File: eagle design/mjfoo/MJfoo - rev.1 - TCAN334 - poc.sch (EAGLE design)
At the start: 3 parts, among them J1 CAN, J2 Power Supply

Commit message: - updated MJfoo to rev. 1a
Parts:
- added 3V3: 3V3, pinhead:PINHD-1X2
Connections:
- net 3V3: now also 3V3.2
- net GND: now also 3V3.1

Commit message: - new programming adapter
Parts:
- removed 3V3: 3V3, pinhead:PINHD-1X2
- removed SWD101: TC2030-NL, tag-connect:TC2030
- added J3: CAN, con-amp:MTA02-100
- added JP1: 3V3, pinhead:PINHD-1X2
- J1: value CAN -> Power Supply
- J2: value Power Supply -> FTSH-107-01-L-DV-K-A; device con-amp:MTA02-100 -> STM32 JTAG 1.27mm 14pin header:FTSH-107-01-L-DV-K-A
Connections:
- new net PB0: JP1.1
- new net PB1: JP1.2
- net 3V3: now also J2.T_VCC_P3, JP1.2; no longer 3V3.2, SWD101.1_T_VCC
- net BAT+: now also J1.2; no longer J2.2
- net CAN_H: now also J3.1; no longer J1.1
- net CAN_L: now also J3.2; no longer J1.2
- net GND: now also J1.1, J2.GND-DETECT_P11, J2.GND_P5, J2.GND_P7, JP1.1; no longer 3V3.1, J2.1, SWD101.5_GND
- net SYS_NRST: now also J2.T_NRST_P12; no longer SWD101.3_T-NRST
- net SYS_SWCLK: now also J2.T_JCLK/T_SWCLK_P6; no longer SWD101.4_T-SWCLK
- net SYS_SWDIO: now also J2.TJTMS/T_SWDIO_P4; no longer SWD101.2_T-SWDIO
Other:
- moved on the sheet: J1

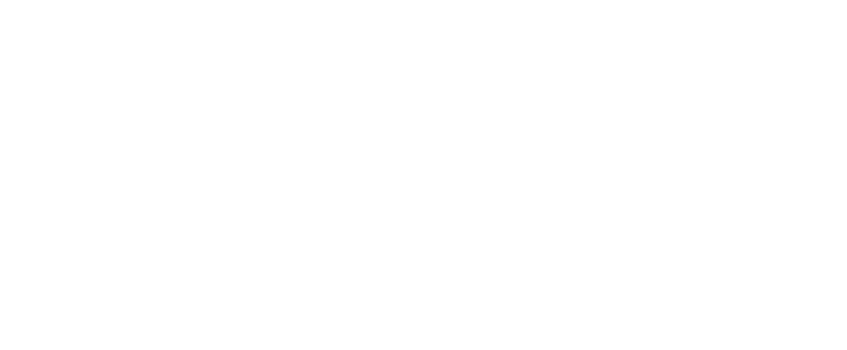
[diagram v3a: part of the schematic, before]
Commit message: updated mjfoo board (was also missing after merge from mj514 branch)
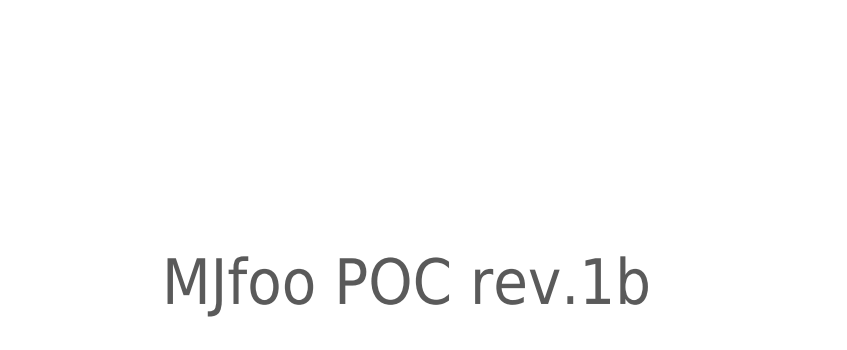
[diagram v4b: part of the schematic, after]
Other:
- note added: "MJfoo POC rev.1b"
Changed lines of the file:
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@@
 <wire x1="10.16" y1="43.18" x2="248.92" y2="43.18" width="0.1524" layer="98" style="dashdot"/>
 <text x="15.24" y="205.74" size="6.4516" layer="98" rot="R180" align="bottom-right">MJ8x8 - generic</text>
+<text x="292.1" y="12.7" size="5.08" layer="97">MJfoo POC rev.1b</text>
 </plain>
 <moduleinsts>

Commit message: MJ818 SuperNova Mini2: - added position key into PCB and spacers; updated gerber, dwg and stl
mj513 - grip:
- corrected bushing dimensions

in mj8x8-foo:
- minor corrections

general board-wide effort:
- replaced pinhead with 0.9mm TH
- added 2nd CAN H & L solder contact
- unified sch nets and drawings

in mj8x8 foo:
- developed rev.1b mj-foo device with voltage detector and CAN TVS protection

in mj808 design:
- updated front led shunt resistor to 0.18 Ohm

in mj8x8:
- added HR30-6R-6P - PushPull Receptacle.lbr receptable
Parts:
- removed J2: FTSH-107-01-L-DV-K-A, STM32 JTAG 1.27mm 14pin header:FTSH-107-01-L-DV-K-A
- removed J3: CAN, con-amp:MTA02-100
- removed JP1: 3V3, pinhead:PINHD-1X2
- added CONN1: HR30-6R-6P(71), HR30-6R-6P - PushPull Receptacle:HR-30-6R-6X
- added TP1: LiIon + Terminal, signal testpoint:TPTH-0.9
- added TP2, TP3, TP4: LiIon - Terminal, signal testpoint:TPTH-0.9
- added TP5, TP6: CAN high, signal testpoint:TPTH-0.9
- added TP7, TP8: CAN low, signal testpoint:TPTH-0.9
- J1: value Power Supply -> FTSH-107-01-L-DV-K-A; device con-amp:MTA02-100 -> STM32 JTAG 1.27mm 14pin header:FTSH-107-01-L-DV-K-A
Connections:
- removed net PB0: JP1.1
- removed net PB1: JP1.2
- net 3V3: now also J1.T_VCC_P3, TP3.TP$1; no longer J2.T_VCC_P3, JP1.2
- net BAT+: now also CONN1.6, TP1.TP$1; no longer J1.2
- net CAN_H: now also CONN1.4, CONN1.5, TP5.TP$1, TP6.TP$1; no longer J3.1
- net CAN_L: now also CONN1.2, CONN1.3, TP7.TP$1, TP8.TP$1; no longer J3.2
- net GND: now also CONN1.1, J1.GND-DETECT_P11, J1.GND_P5, J1.GND_P7, TP2.TP$1, TP4.TP$1; no longer J1.1, J2.GND-DETECT_P11, J2.GND_P5, J2.GND_P7, JP1.1
- net SYS_NRST: now also J1.T_NRST_P12; no longer J2.T_NRST_P12
- net SYS_SWCLK: now also J1.T_JCLK/T_SWCLK_P6; no longer J2.T_JCLK/T_SWCLK_P6
- net SYS_SWDIO: now also J1.TJTMS/T_SWDIO_P4; no longer J2.TJTMS/T_SWDIO_P4
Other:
- note added: "2"
- note added: "3"
- note added: "4"
- note added: "5"
- note added: "inbound, brown"
- note added: "inbound, white"
- note added: "outbound, brown"
- note added: "outbound, white"
